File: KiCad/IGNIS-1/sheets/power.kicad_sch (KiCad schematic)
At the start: 10 parts, among them J1 LiPo_1S_in, J2 RBF_pin, SW1 Main_SW, U1 Prot_1S_UVLO_OCP, U2 BuckBoost_3V3, U3 Boost_5V

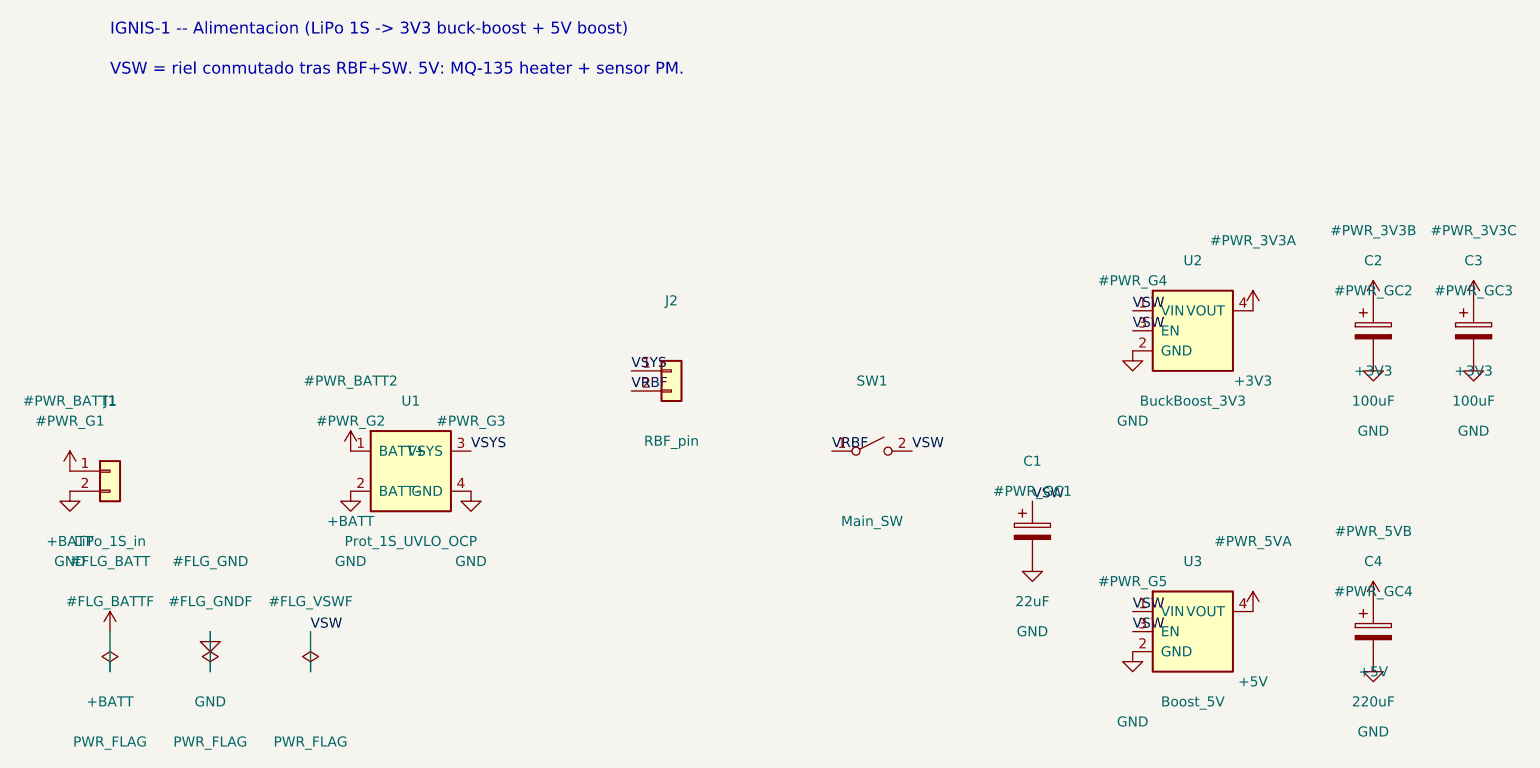
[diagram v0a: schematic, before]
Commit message: Actualizado los boards de IGNIS - separado en 3 boards
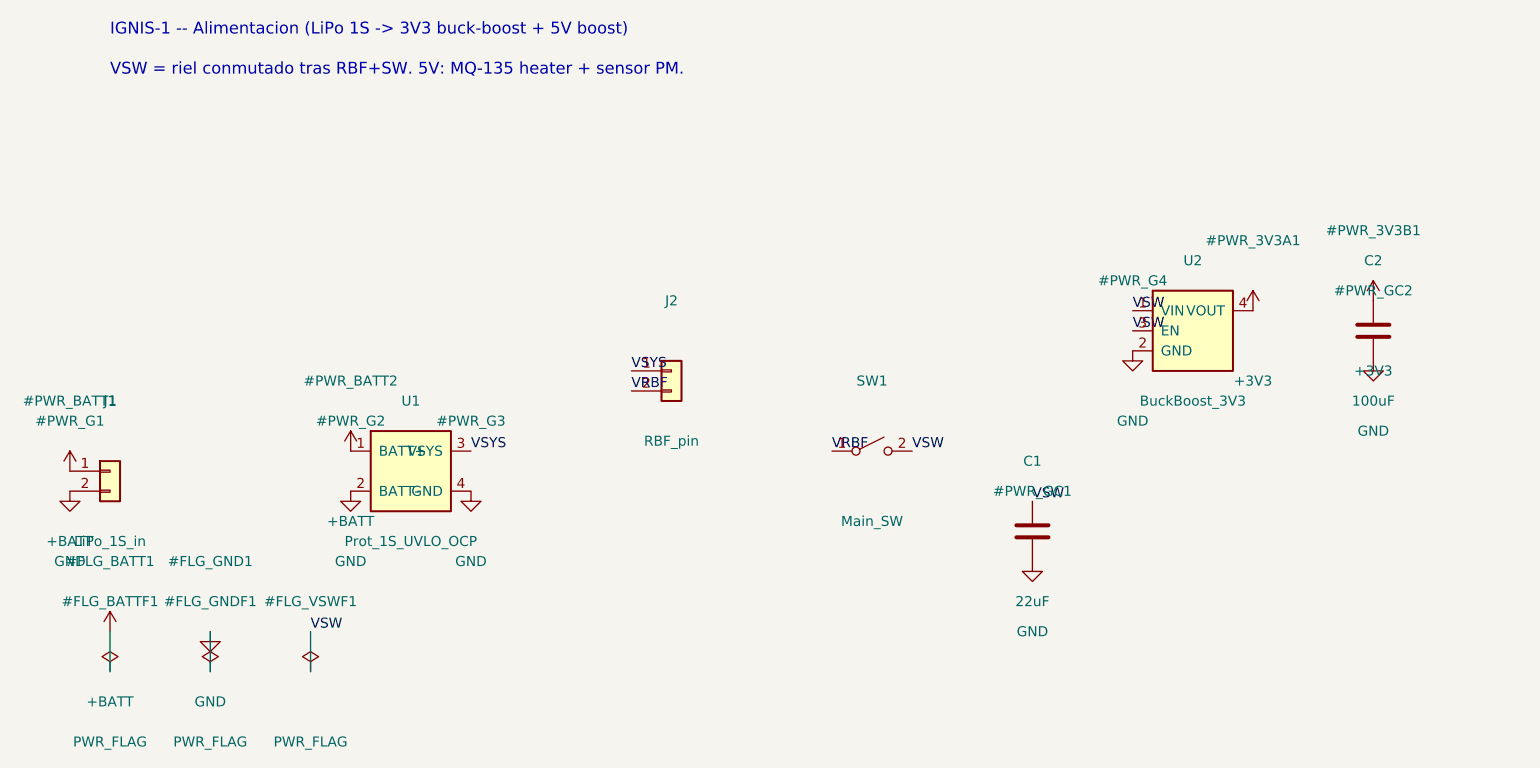
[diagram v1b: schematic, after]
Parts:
- removed C1: 22uF, Capacitor_THT:CP_Radial_D6.3mm_P2.50mm, symbol Device:C_Polarized
- removed C2, C3: 100uF, Capacitor_THT:CP_Radial_D6.3mm_P2.50mm, symbol Device:C_Polarized
- removed C4: 220uF, Capacitor_THT:CP_Radial_D6.3mm_P2.50mm, symbol Device:C_Polarized
- removed U3: Boost_5V, symbol IGNIS1:DCDC_Module
- added C1: 22uF, Capacitor_SMD:C_0805_2012Metric, symbol Device:C
- added C2: 100uF, Capacitor_SMD:C_1210_3225Metric, symbol Device:C
- U1, U2: footprint (none) -> Connector_PinHeader_2.54mm:PinHeader_1x04_P2.54mm_Vertical
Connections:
- net +3V3: now also C2.1
- net GND: now also C1.2, C2.2
- net VSW: now also C1.1
